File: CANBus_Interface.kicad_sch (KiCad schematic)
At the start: 27 parts, among them U701 TCAN4550-Q1, U702 74LV1T125, Y701 40MHz

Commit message: Update .gitignore, CANBus_Interface.kicad_sch, ESP32-S3_WLED_UnderGlow_Hat-2026-05-04_233126.zip, and 17 more files
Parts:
- removed C704, C706, C707, C708, C709, C710: 22uF, My Capacitors:C_0603_Dense, symbol Device:C_Small
- removed C711: 0.1uF, My Capacitors:C_0201_Dense, symbol Device:C_Small
- added C704, C706, C707, C708, C709, C710: 22uF, My Capacitors:C_0603_Dense, symbol Device:C
- added C711: 0.1uF, My Capacitors:C_0201_Dense, symbol Device:C
- C701, C702, C703, C705, C713, C714, C715, C716: symbol Device:C_Small -> Device:C
- Y701: Distributor Link  2 https://www.mouser.com/ProductDetail/ABRACON/ASAAIG-40.000M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 -> (none); Distributor Link 2 (none) -> https://www.mouser.com/ProductDetail/ABRACON/ASAAIG-40.000M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
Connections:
- net +3V3: now also C711.1
- net +V_{SUP}: now also C707.1, C708.1, C709.1, C710.1
- net GND: now also C704.2, C706.2, C707.2, C708.2, C709.2, C710.2, C711.2
- net V_{CC_{OUT}}: now also C704.1, C706.1
- net FLTR: no longer names the net of C713.1, C714.1, C715.1, C716.1, U701.18 (FLTR)
- net OSC1: no longer names the net of U701.1 (OSC1), Y701.3 (OUT)
- net RST: no longer names the net of R704.2, U701.19 (RST), U702.4 (Y)
- net SDO_{CAN} renamed SDO_{raw}
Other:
- moved on the sheet: D702, D703

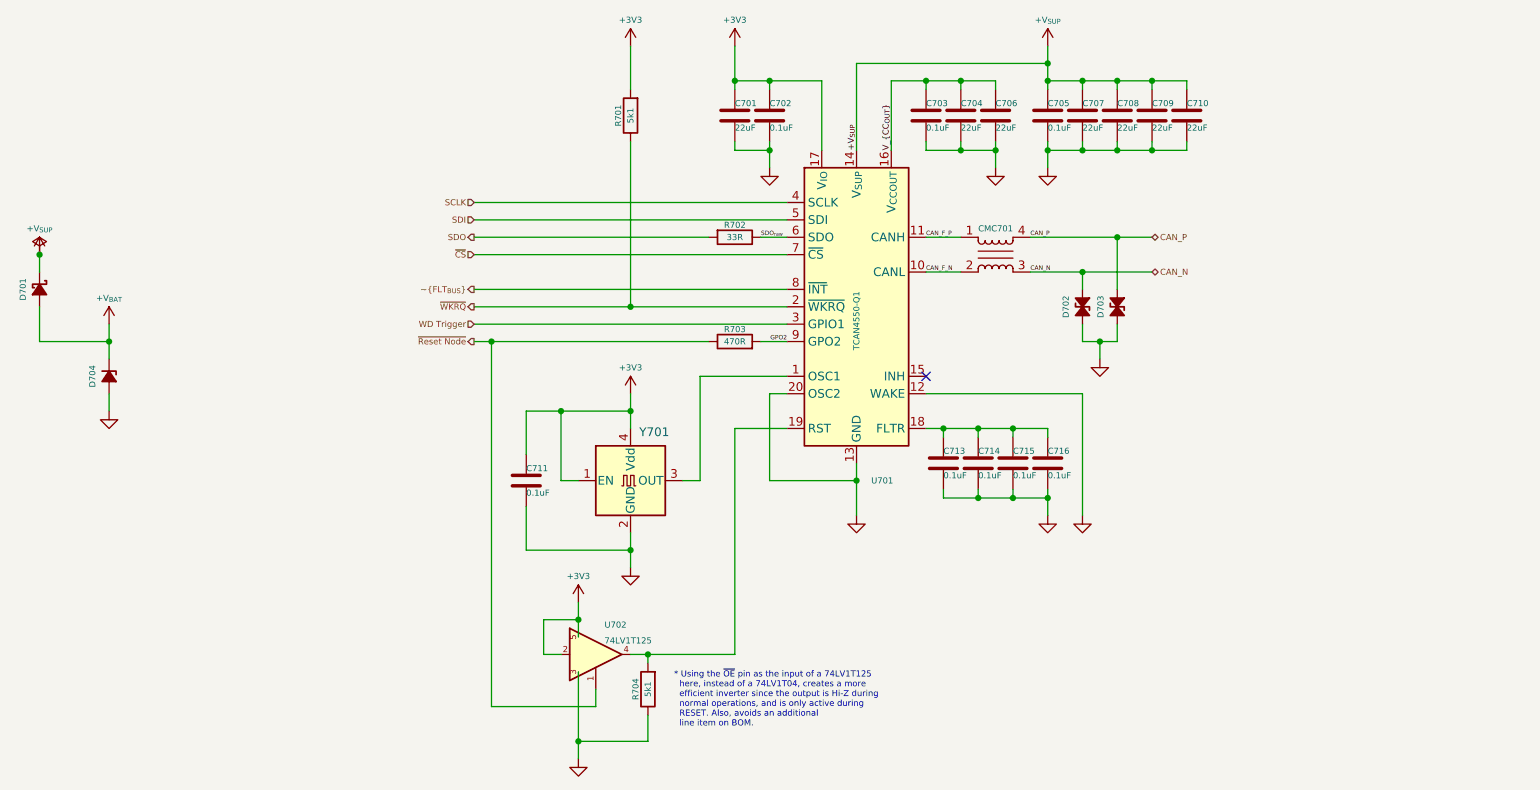
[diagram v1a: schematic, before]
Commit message: replaced Device:C with Device:C_Small and Device:R with Device:R_Small
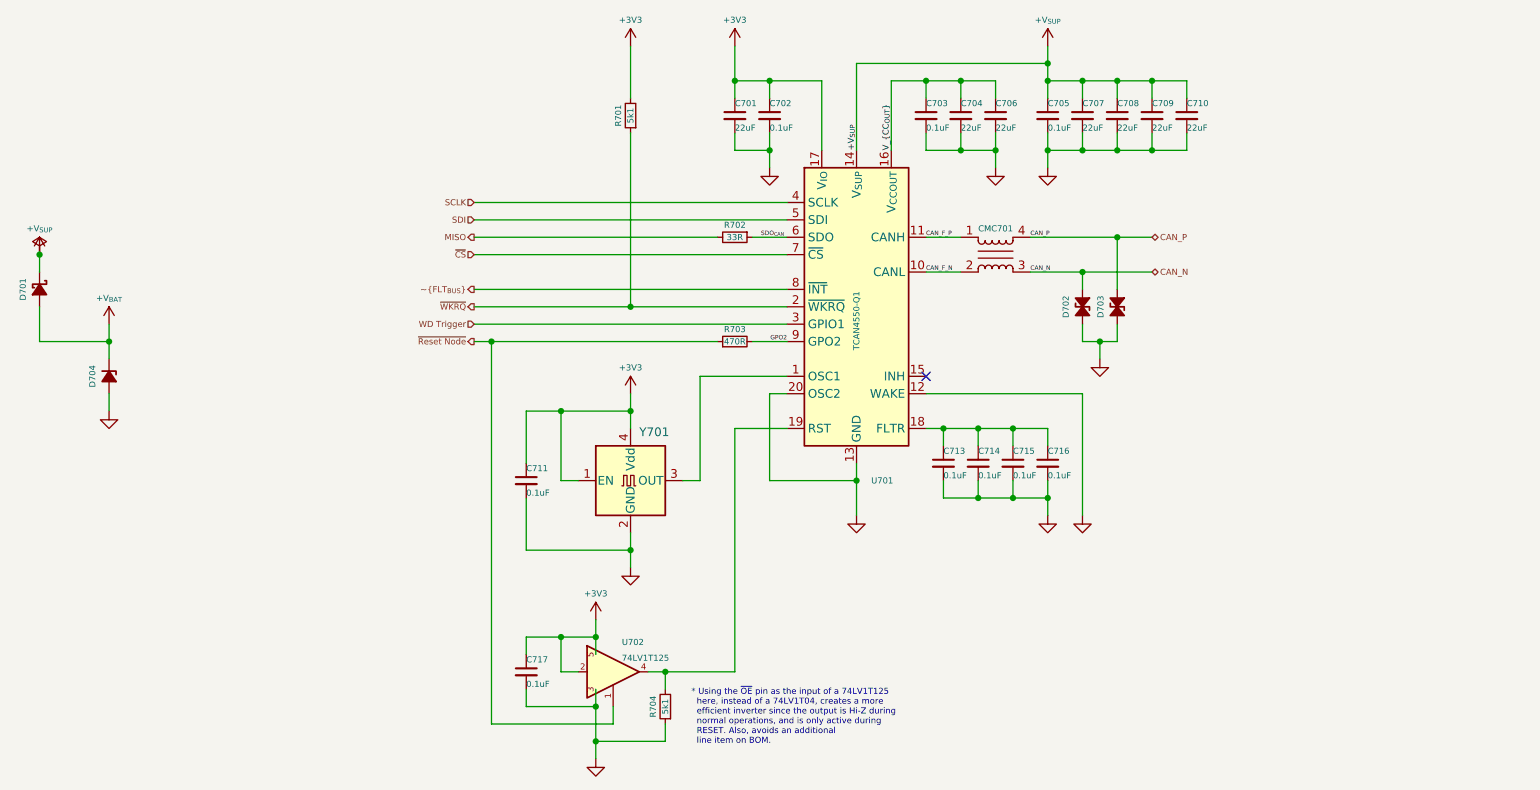
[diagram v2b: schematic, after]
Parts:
- added C717: 0.1uF, My Capacitors:C_0201_Dense, symbol Device:C_Small
- C701, C702, C703, C704, C705, C706, C707, C708, C709, C710, C711, C713, C714, C715, C716: symbol Device:C -> Device:C_Small
- R701, R702, R703, R704: symbol Device:R -> Device:R_Small
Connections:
- net +3V3: now also C717.1
- net GND: now also C717.2
- net SDO renamed MISO
- net SDO_{raw} renamed SDO_{CAN}
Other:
- moved on the sheet: R704, U702

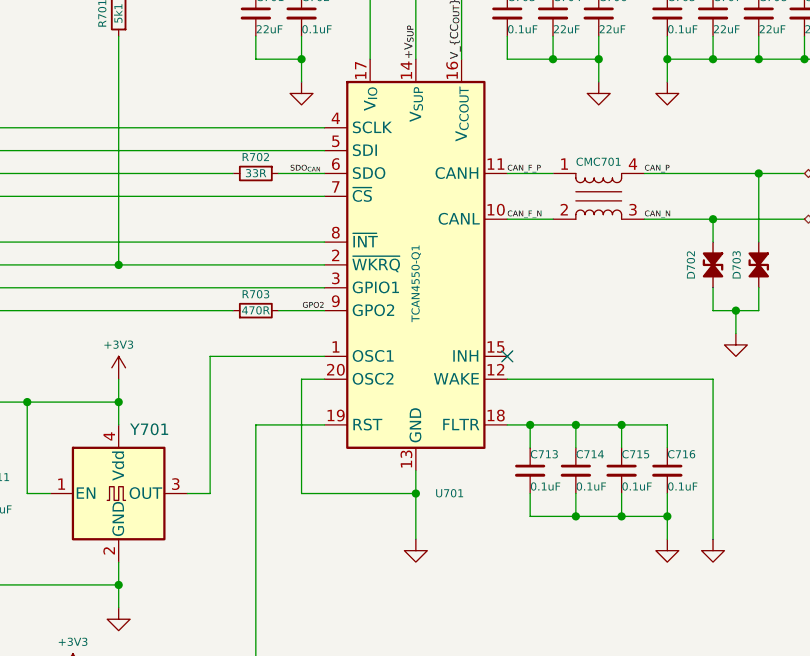
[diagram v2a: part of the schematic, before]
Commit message: schematic updated with new ESP32-S3_D1_Pico symbol
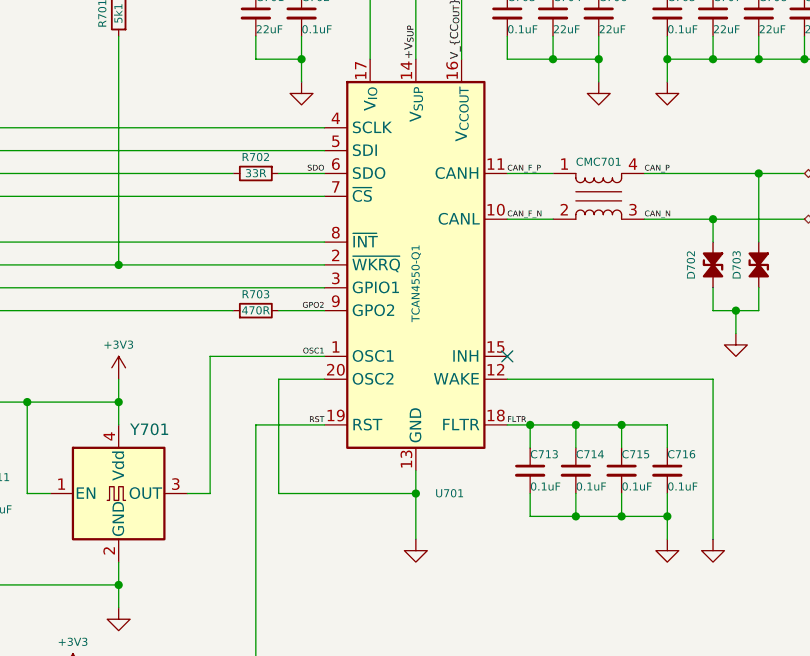
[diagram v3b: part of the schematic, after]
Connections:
- net OSC1: now reaches U701.1 (OSC1), Y701.3 (OUT)
- net FLTR: now reaches C713.1, C714.1, C715.1, C716.1, U701.18 (FLTR)
- net RST: now reaches R704.2, U701.19 (RST), U702.4 (Y)
- net SDO_{CAN} renamed SDO
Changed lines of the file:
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@@
 	(wire
 		(pts
-			(xy 137.16 106.68) (xy 134.62 106.68)
+			(xy 137.16 106.68) (xy 132.08 106.68)
 		)
 		(stroke
@@
 	(wire
 		(pts
-			(xy 134.62 119.38) (xy 147.32 119.38)
+			(xy 132.08 119.38) (xy 147.32 119.38)
 		)
 		(stroke
@@
 	(wire
 		(pts
-			(xy 134.62 106.68) (xy 134.62 119.38)
+			(xy 132.08 106.68) (xy 132.08 119.38)
 		)
 		(stroke
@@
 			(width 0)
 			(type default)
+		)
+	)
+	(label "FLTR"
+		(at 157.48 111.76 0)
+		(effects
+			(font
+				(size 0.635 0.635)
+			)
+			(justify left bottom)
 		)
 	)
@@
 		)
 	)
+	(label "RST"
+		(at 137.16 111.76 180)
+		(effects
+			(font
+				(size 0.635 0.635)
+			)
+			(justify right bottom)
+		)
+	)
 	(label "CAN_F_N"
 		(at 157.48 88.9 0)
@@
 		)
 	)
-	(label "SDO_{CAN}"
-		(at 133.35 83.82 0)
-		(effects
-			(font
-				(size 0.635 0.635)
-			)
-			(justify left bottom)
+	(label "SDO"
+		(at 137.16 83.82 180)
+		(effects
+			(font
+				(size 0.635 0.635)
+			)
+			(justify right bottom)
 		)
 	)
@@
 		)
 	)
+	(label "OSC1"
+		(at 137.16 104.14 180)
+		(effects
+			(font
+				(size 0.635 0.635)
+			)
+			(justify right bottom)
+		)
+	)

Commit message: JLCPCB: W2026061412450502 2026-06-14 PCB: Y62-5297522A PCBA: SMT026061460215-5297522A
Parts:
- added +V11, +V12, +V14, +V16, +V19: +3V3, symbol My Power Management:+V (Local)
- added +V13, +V15: +V_{SUP}, symbol My Power Management:+V (Local)
- added +V17, +V18: +V_{BAT}, symbol My Power Management:+V (Local)
- added GND10, GND11, GND12, GND13, GND14, GND15, GND16, GND17, GND7, GND8, GND9: GND, symbol My Power Management:GND (Local)
- D701: footprint Personal_FootprintLibrary:DSN0603-2 -> My Package_Leadless:DFN0603-2
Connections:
- net +3V3: now also +V11.1, +V12.1, +V14.1, +V16.1, +V19.1
- net +V_{BAT}: now also +V17.1, +V18.1
- net +V_{SUP}: now also +V13.1, +V15.1
- net GND: now also GND10.1 (GND), GND11.1 (GND), GND12.1 (GND), GND13.1 (GND), GND14.1 (GND), GND15.1 (GND), GND16.1 (GND), GND17.1 (GND), GND7.1 (GND), GND8.1 (GND), GND9.1 (GND)
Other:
- moved on the sheet: D701, D704
